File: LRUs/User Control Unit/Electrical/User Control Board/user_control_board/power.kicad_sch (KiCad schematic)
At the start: 1 part, among them J3 Screw_Terminal_01x02

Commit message: hello
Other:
- added sheet 3.3V (untitled.kicad_sch)
- title: (none) -> Power
- moved on the sheet: J3
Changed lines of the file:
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@@
 	(generator_version "10.0")
 	(paper "A4")
-	(wire
-		(pts
-			(xy 123.19 67.31) (xy 118.11 67.31)
-		)
-		(stroke
-			(width 0)
-			(type default)
-		)
-	)
-	(wire
-		(pts
-			(xy 52.07 67.31) (xy 87.63 67.31)
-		)
-		(stroke
-			(width 0)
-			(type default)
-		)
-	)
-	(wire
-		(pts
-			(xy 123.19 64.77) (xy 123.19 67.31)
-		)
-		(stroke
-			(width 0)
-			(type default)
-		)
-	)
-	(wire
-		(pts
-			(xy 54.61 72.39) (xy 54.61 69.85)
-		)
-		(stroke
-			(width 0)
-			(type default)
-		)
-	)
-	(wire
-		(pts
-			(xy 54.61 69.85) (xy 52.07 69.85)
+	(title_block
+		(title "Power")
+	)
+	(wire
+		(pts
+			(xy 133.35 71.12) (xy 128.27 71.12)
+		)
+		(stroke
+			(width 0)
+			(type default)
+		)
+	)
+	(wire
+		(pts
+			(xy 62.23 71.12) (xy 97.79 71.12)
+		)
+		(stroke
+			(width 0)
+			(type default)
+		)
+	)
+	(wire
+		(pts
+			(xy 133.35 68.58) (xy 133.35 71.12)
+		)
+		(stroke
+			(width 0)
+			(type default)
+		)
+	)
+	(wire
+		(pts
+			(xy 64.77 76.2) (xy 64.77 73.66)
+		)
+		(stroke
+			(width 0)
+			(type default)
+		)
+	)
+	(wire
+		(pts
+			(xy 64.77 73.66) (xy 62.23 73.66)
 		)
 		(stroke
@@
 	(symbol
 		(lib_id "power:+5V")
-		(at 123.19 64.77 0)
+		(at 133.35 68.58 0)
 		(unit 1)
 		(body_style 1)
@@
 		(fields_autoplaced yes)
 		(property "Reference" "#PWR04"
-			(at 123.19 68.58 0)
+			(at 133.35 72.39 0)
 			(hide yes)
 			(show_name no)
@@
 		)
 		(property "Value" "+5V"
-			(at 123.19 59.69 0)
+			(at 133.35 63.5 0)
 			(show_name no)
 			(do_not_autoplace no)
@@
 		)
 		(property "Footprint" ""
-			(at 123.19 64.77 0)
+			(at 133.35 68.58 0)
 			(hide yes)
 			(show_name no)
@@
 		)
 		(property "Datasheet" ""
-			(at 123.19 64.77 0)
+			(at 133.35 68.58 0)
 			(hide yes)
 			(show_name no)
@@
 		)
 		(property "Description" "Power symbol creates a global label with name \"+5V\""
-			(at 123.19 64.77 0)
+			(at 133.35 68.58 0)
 			(hide yes)
 			(show_name no)
@@
 	(symbol
 		(lib_id "power:GND")
-		(at 54.61 72.39 0)
+		(at 64.77 76.2 0)
 		(unit 1)
 		(body_style 1)
@@
 		(fields_autoplaced yes)
 		(property "Reference" "#PWR03"
-			(at 54.61 78.74 0)
+			(at 64.77 82.55 0)
 			(hide yes)
 			(show_name no)
@@
 		)
 		(property "Value" "GND"
-			(at 54.61 77.47 0)
+			(at 64.77 81.28 0)
 			(hide yes)
 			(show_name no)
@@
 		)
 		(property "Footprint" ""
-			(at 54.61 72.39 0)
+			(at 64.77 76.2 0)
 			(hide yes)
 			(show_name no)
@@
 		)
 		(property "Datasheet" ""
-			(at 54.61 72.39 0)
+			(at 64.77 76.2 0)
 			(hide yes)
 			(show_name no)
@@
 		)
 		(property "Description" "Power symbol creates a global label with name \"GND\" , ground"
-			(at 54.61 72.39 0)
+			(at 64.77 76.2 0)
 			(hide yes)
 			(show_name no)
@@
 	(symbol
 		(lib_id "Connector:Screw_Terminal_01x02")
-		(at 46.99 67.31 0)
+		(at 57.15 71.12 0)
 		(mirror y)
 		(unit 1)
@@
 		(fields_autoplaced yes)
 		(property "Reference" "J3"
-			(at 46.99 60.96 0)
+			(at 57.15 64.77 0)
 			(show_name no)
 			(do_not_autoplace no)
@@
 		)
 		(property "Value" "Screw_Terminal_01x02"
-			(at 46.99 63.5 0)
+			(at 57.15 67.31 0)
 			(show_name no)
 			(do_not_autoplace no)
@@
 		)
 		(property "Footprint" "TerminalBlock_Phoenix:TerminalBlock_Phoenix_MPT-0,5-2-2.54_1x02_P2.54mm_Horizontal"
-			(at 46.99 67.31 0)
+			(at 57.15 71.12 0)
 			(hide yes)
 			(show_name no)
@@
 		)
 		(property "Datasheet" ""
-			(at 46.99 67.31 0)
+			(at 57.15 71.12 0)
 			(hide yes)
 			(show_name no)
@@
 		)
 		(property "Description" "Generic screw terminal, single row, 01x02, script generated (kicad-library-utils/schlib/autogen/connector/)"
-			(at 46.99 67.31 0)
+			(at 57.15 71.12 0)
 			(hide yes)
 			(show_name no)
@@
 	)
 	(sheet
-		(at 87.63 64.77)
-		(size 30.48 17.78)
+		(at 213.36 76.2)
+		(size 66.04 30.48)
 		(exclude_from_sim no)
 		(in_bom yes)
@@
 			(color 255 255 194 1)
 		)
+		(property "Sheetname" "3.3V"
+			(at 213.36 75.4884 0)
+			(show_name no)
+			(do_not_autoplace no)
+			(effects
+				(font
+					(size 1.27 1.27)
+				)
+				(justify left bottom)
+			)
+		)
+		(property "Sheetfile" "untitled.kicad_sch"
+			(at 213.36 107.2646 0)
+			(show_name no)
+			(do_not_autoplace no)
+			(effects
+				(font
+					(size 1.27 1.27)
+				)
+				(justify left top)
+			)
+		)
+		(pin "fjkldsjflks" input
+			(at 246.38 106.68 270)
+			(effects
+				(font
+					(size 1.27 1.27)
+				)
+				(justify left)
+			)
+		)
+		(instances
+			(project "user_control_board"
+				(path "/4e4fbe8c-7357-4f75-8a99-a243261c2770"
+					(page "7")
+				)
+			)
+		)
+	)
+	(sheet
+		(at 97.79 68.58)
+		(size 30.48 17.78)
+		(exclude_from_sim no)
+		(in_bom yes)
+		(on_board yes)
+		(dnp no)
+		(fields_autoplaced yes)
+		(stroke
+			(width 0.3048)
+			(type solid)
+		)
+		(fill
+			(color 255 255 194 1)
+		)
 		(property "Sheetname" "5V"
-			(at 87.63 63.9822 0)
+			(at 97.79 67.7922 0)
 			(show_name no)
 			(do_not_autoplace no)
@@
 		)
 		(property "Sheetfile" "5V.kicad_sch"
-			(at 87.63 83.2108 0)
+			(at 97.79 87.0208 0)
 			(show_name no)
 			(do_not_autoplace no)
@@
 		)
 		(pin "VIN" input
-			(at 87.63 67.31 180)
+			(at 97.79 71.12 180)
 			(effects
 				(font
@@
 		)
 		(pin "5V_MAIN_PG" output
-			(at 118.11 73.66 0)
+			(at 128.27 77.47 0)
 			(effects
 				(font
@@
 		)
 		(pin "VOUT" output
-			(at 118.11 67.31 0)
-			(effects
-				(font
+			(at 128.27 71.12 0)
+			(effects
+				(font

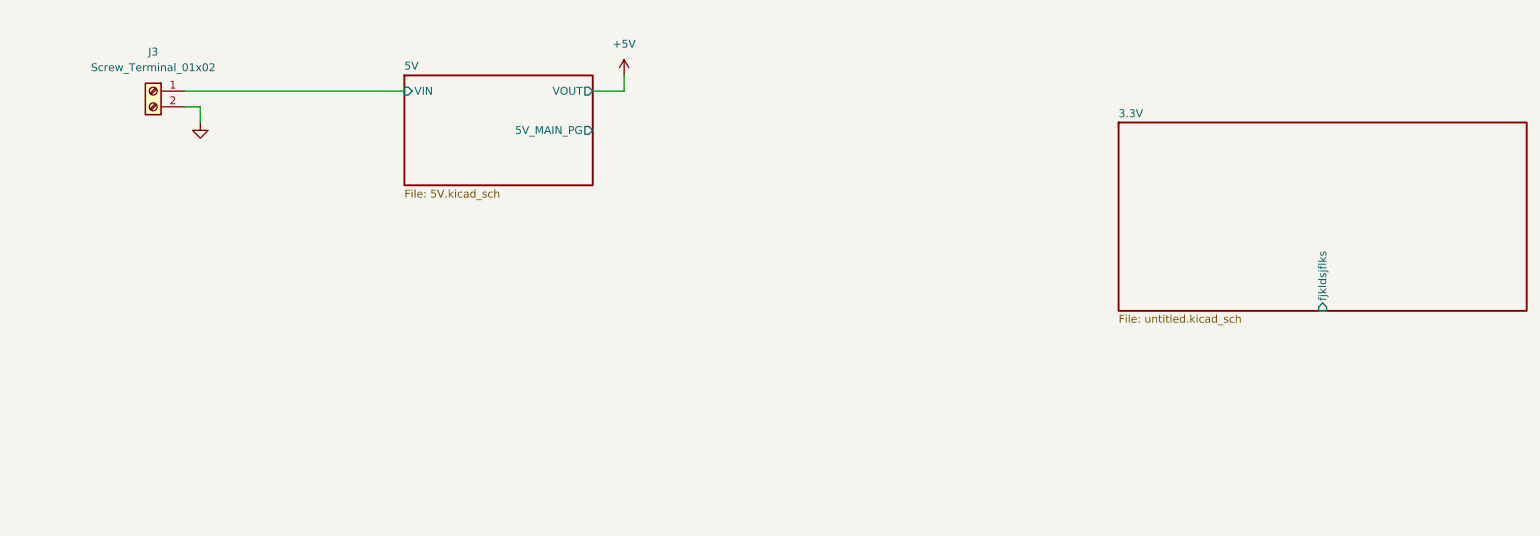
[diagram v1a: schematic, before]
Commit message: Added 12V XL6009 boost converter schematic
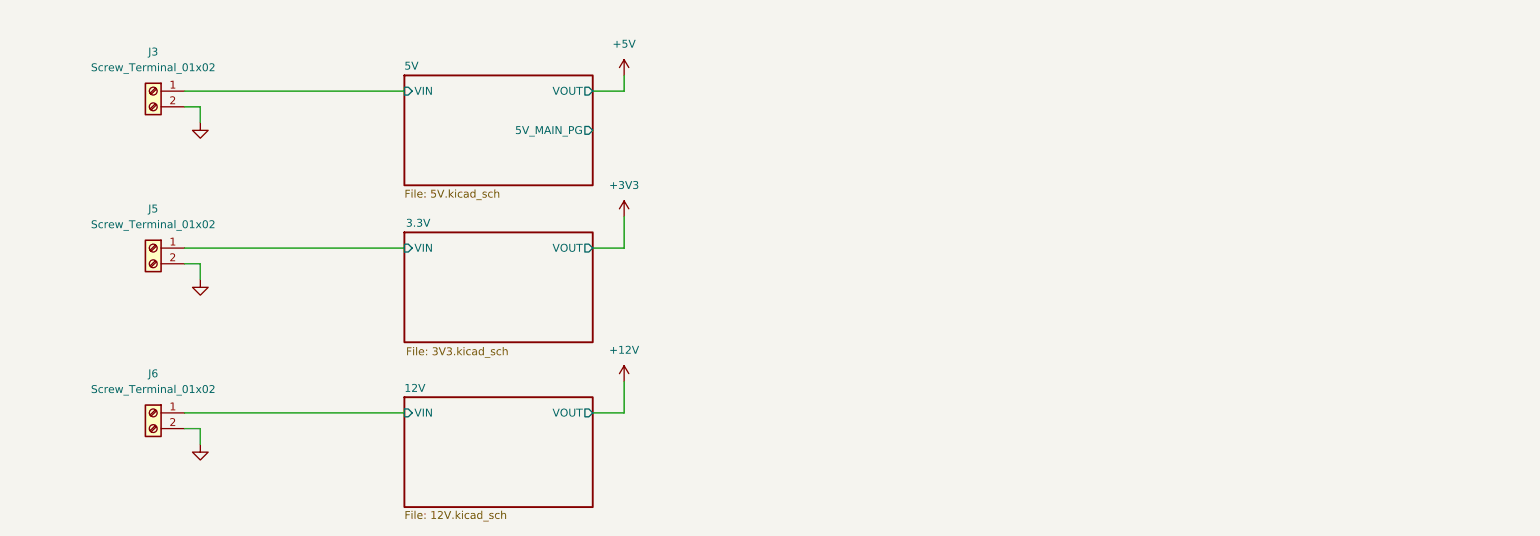
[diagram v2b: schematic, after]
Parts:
- added J5, J6: Screw_Terminal_01x02, TerminalBlock_Phoenix:TerminalBlock_Phoenix_MPT-0,5-2-2.54_1x02_P2.54mm_Horizontal, symbol Connector:Screw_Terminal_01x02
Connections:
- net GND: now also J5.2 (Pin_2), J6.2 (Pin_2)
- new net 12V/VIN: J6.1 (Pin_1)
- new net 3.3V/VIN: J5.1 (Pin_1)
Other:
- added sheet 12V (12V.kicad_sch)
- sheet 3.3V: file untitled.kicad_sch -> 3V3.kicad_sch
- sheet 3.3V ports: added VIN, VOUT; removed fjkldsjflks

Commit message: DAC added Removed unnecessary modules.
Need to make custom footprint for dac.
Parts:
- removed J6: Screw_Terminal_01x02, TerminalBlock_Phoenix:TerminalBlock_Phoenix_MPT-0,5-2-2.54_1x02_P2.54mm_Horizontal, symbol Connector:Screw_Terminal_01x02
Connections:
- net 5V/VIN is gone; now on an unnamed net: J3.1 (Pin_1)
- net 12V/VIN: now also J5.2 (Pin_2)
- net GND: no longer J5.2 (Pin_2)
- net 3.3V/VIN: no longer names the net of J5.1 (Pin_1)

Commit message: footprint and added symbol for audio
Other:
- note added: "2S Battery"
- note added: "Fuse"
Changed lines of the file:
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@@
 		(title "Power")
+	)
+	(text "2S Battery\n"
+		(exclude_from_sim no)
+		(at 55.118 61.722 0)
+		(effects
+			(font
+				(size 1.27 1.27)
+			)
+		)
+	)
+	(text "Fuse"
+		(exclude_from_sim no)
+		(at 61.976 88.138 0)
+		(effects
+			(font
+				(size 1.27 1.27)
+			)
+		)
 	)
 	(junction

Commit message: drc run
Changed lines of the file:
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@@
-	)
-	(junction
-		(at 97.79 123.19)
-		(diameter 0)
-		(color 0 0 0 0)
 	)
 	(junction
@@
 		(diameter 0)
 		(color 0 0 0 0)
-	)
-	(wire
-		(pts
-			(xy 88.9 123.19) (xy 97.79 123.19)
-		)
-		(stroke
-			(width 0)
-			(type default)
-		)
 	)
 	(wire
@@
 	(wire
 		(pts
+			(xy 88.9 123.19) (xy 97.79 123.19)
+		)
+		(stroke
+			(width 0)
+			(type default)
+		)
+	)
+	(wire
+		(pts
 			(xy 81.28 71.12) (xy 81.28 87.63)
 		)
@@
 		)
 		(stroke
-			(width 0)
-			(type default)
-		)
-	)
-	(wire
-		(pts
-			(xy 97.79 123.19) (xy 99.06 123.19)
-		)
-		(stroke

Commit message: need to run DCR
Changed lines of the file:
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@@
 	(text "2S Battery\n"
 		(exclude_from_sim no)
-		(at 55.118 61.722 0)
+		(at 57.15 61.976 0)
 		(effects
 			(font
@@
 	(text "Fuse"
 		(exclude_from_sim no)
-		(at 61.976 88.138 0)
+		(at 71.12 93.472 0)
 		(effects
 			(font
@@
 		)
 		(property "Sheetname" "12V"
-			(at 97.79 119.9384 0)
+			(at 97.79 119.8622 0)
 			(show_name no)
 			(do_not_autoplace no)
@@
 		)
 		(property "Sheetfile" "12V.kicad_sch"
-			(at 97.79 139.0146 0)
-			(show_name no)
-			(do_not_autoplace no)
+			(at 97.79 139.0908 0)
+			(show_name no)
+			(do_not_autoplace no)

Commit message: connectors and 5v buck partially done
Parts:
- renumbered J5 to J4
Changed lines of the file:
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@@
+	(wire
+		(pts
+			(xy 128.27 77.47) (xy 135.89 77.47)
+		)
+		(stroke
+			(width 0)
+			(type default)
+		)
+	)
 	(wire
 		(pts
@@
 	(wire
 		(pts
-			(xy 133.35 68.58) (xy 133.35 71.12)
+			(xy 133.35 67.31) (xy 133.35 71.12)
 		)
 		(stroke
@@
 			(width 0)
 			(type default)
+		)
+	)
+	(global_label "PG"
+		(shape output)
+		(at 135.89 77.47 0)
+		(fields_autoplaced yes)
+		(effects
+			(font
+				(size 1.27 1.27)
+			)
+			(justify left)
+		)
+		(property "Intersheetrefs" "${INTERSHEET_REFS}"
+			(at 141.4152 77.47 0)
+			(hide yes)
+			(show_name no)
+			(do_not_autoplace no)
+			(effects
+				(font
+					(size 1.27 1.27)
+				)
+				(justify left)
+			)
 		)
 	)
 	(symbol
 		(lib_id "power:+5V")
-		(at 133.35 68.58 0)
+		(at 133.35 67.31 0)
 		(unit 1)
 		(body_style 1)
@@
 		(dnp no)
 		(fields_autoplaced yes)
-		(property "Reference" "#PWR04"
-			(at 133.35 72.39 0)
+		(property "Reference" "#PWR027"
+			(at 133.35 71.12 0)
 			(hide yes)
 			(show_name no)
@@
 		)
 		(property "Value" "+5V"
-			(at 133.35 63.5 0)
+			(at 133.35 62.23 0)
 			(show_name no)
 			(do_not_autoplace no)
@@
 		)
 		(property "Footprint" ""
-			(at 133.35 68.58 0)
+			(at 133.35 67.31 0)
 			(hide yes)
 			(show_name no)
@@
 		)
 		(property "Datasheet" ""
-			(at 133.35 68.58 0)
+			(at 133.35 67.31 0)
 			(hide yes)
 			(show_name no)
@@
 		)
 		(property "Description" "Power symbol creates a global label with name \"+5V\""
-			(at 133.35 68.58 0)
+			(at 133.35 67.31 0)
 			(hide yes)
 			(show_name no)
@@
 			(project "user_control_board"
 				(path "/4e4fbe8c-7357-4f75-8a99-a243261c2770"
-					(reference "#PWR04")
+					(reference "#PWR027")
 					(unit 1)
 				)
@@
 		(dnp no)
 		(fields_autoplaced yes)
-		(property "Reference" "#PWR03"
+		(property "Reference" "#PWR026"
 			(at 62.23 82.55 0)
 			(hide yes)
@@
 			(project "user_control_board"
 				(path "/4e4fbe8c-7357-4f75-8a99-a243261c2770"
-					(reference "#PWR03")
+					(reference "#PWR026")
 					(unit 1)
 				)
@@
 		(dnp no)
 		(fields_autoplaced yes)
-		(property "Reference" "#PWR08"
+		(property "Reference" "#PWR028"
 			(at 133.35 95.25 0)
 			(hide yes)
@@
 			(project "user_control_board"
 				(path "/4e4fbe8c-7357-4f75-8a99-a243261c2770"
-					(reference "#PWR08")
+					(reference "#PWR028")
 					(unit 1)
 				)
@@
 		(dnp no)
 		(fields_autoplaced yes)
-		(property "Reference" "J5"
+		(property "Reference" "J4"
 			(at 71.12 81.28 0)
 			(show_name no)
@@
 			(project "user_control_board"
 				(path "/4e4fbe8c-7357-4f75-8a99-a243261c2770"
-					(reference "J5")
+					(reference "J4")
 					(unit 1)
 				)
@@
 		(dnp no)
 		(fields_autoplaced yes)
-		(property "Reference" "#PWR015"
+		(property "Reference" "#PWR029"
 			(at 133.35 121.92 0)
 			(hide yes)
@@
 			(project "user_control_board"
 				(path "/4e4fbe8c-7357-4f75-8a99-a243261c2770"
-					(reference "#PWR015")
+					(reference "#PWR029")
 					(unit 1)
 				)
